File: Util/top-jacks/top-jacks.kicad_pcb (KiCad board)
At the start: 2 copper layers, 50.5 x 32.1 mm, 6 parts, among them J1 Screw_Terminal_01x02, J4 Barrel_Jack_Switch, J5 Screw_Terminal_01x06, J6 Screw_Terminal_01x02

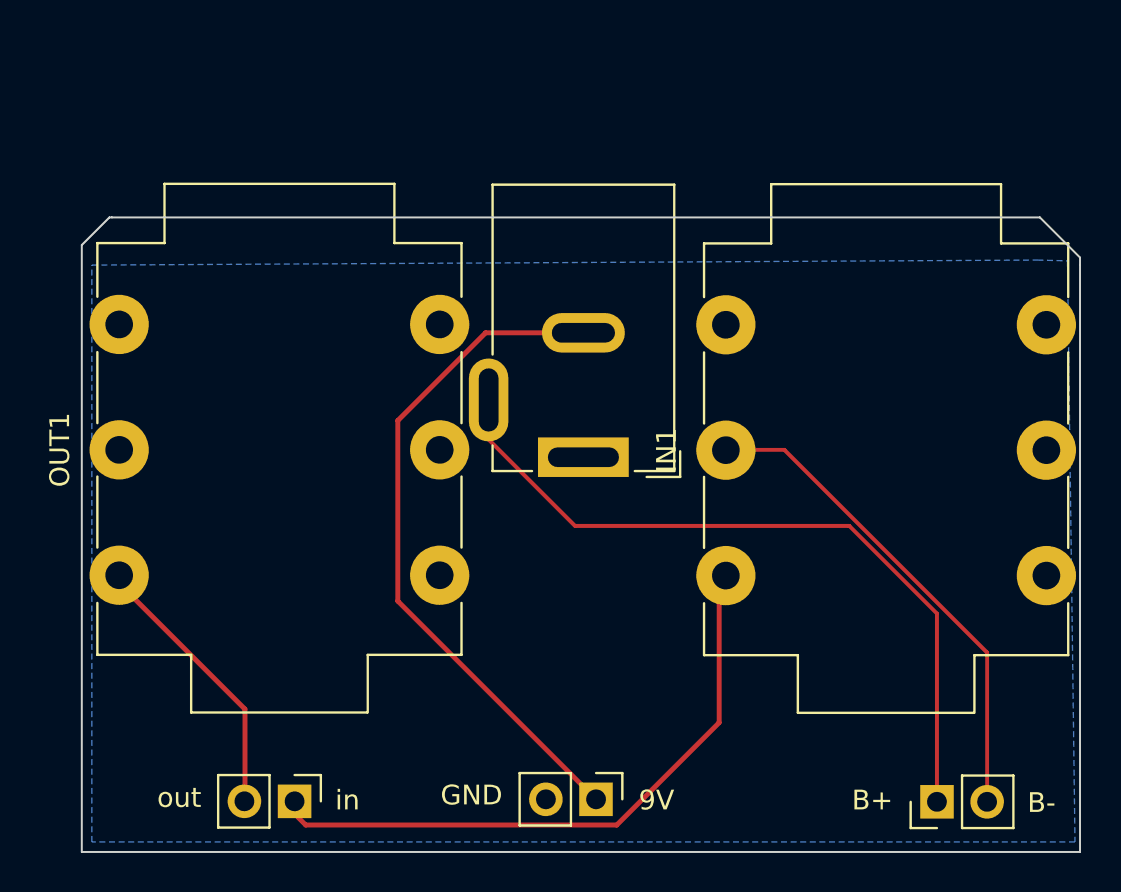
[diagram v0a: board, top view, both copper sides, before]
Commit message: replaced whiefuzz, and modified ejfuzzface
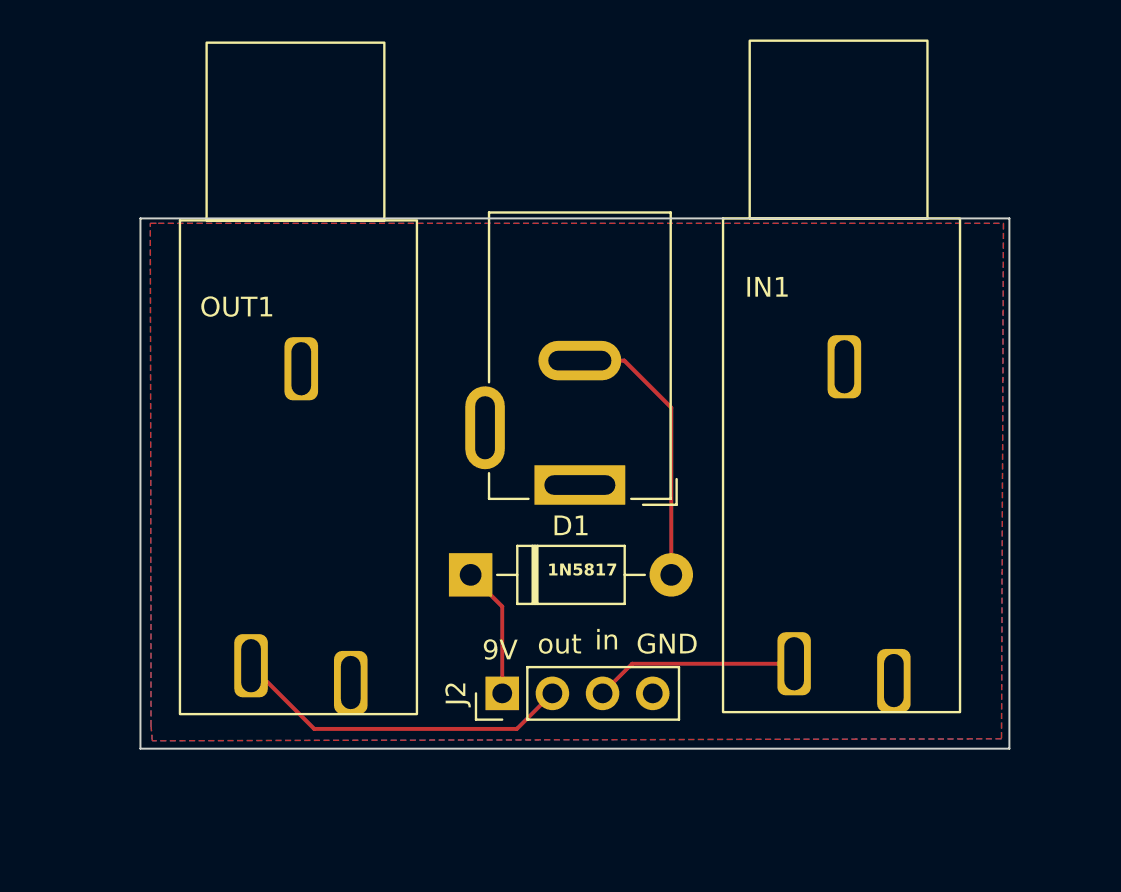
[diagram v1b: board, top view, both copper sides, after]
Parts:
- removed J1, J6: Screw_Terminal_01x02, Connector_PinHeader_2.54mm:PinHeader_1x02_P2.54mm_Vertical
- removed J5: Screw_Terminal_01x06, Connector_PinHeader_2.54mm:PinHeader_1x02_P2.54mm_Vertical
- added D1: 1N5817, Diode_THT:D_DO-41_SOD81_P10.16mm_Horizontal, F.Cu at (69.2, 94.3)
- added J2: Conn_01x04_Socket, Connector_PinHeader_2.54mm:PinHeader_1x04_P2.54mm_Vertical, F.Cu at (70.8, 100.3)
- IN1, OUT1: footprint Connector_Audio:Jack_6.35mm_Neutrik_NMJ6HCD2_Horizontal -> pedals:6.35mm-audio-jack
- moved OUT1 20.1 mm to (60.6, 76.4), turned to 0 degrees
- moved IN1 19.0 mm to (88.1, 76.3), turned to 0 degrees
- moved J4 1.42 mm to (74.8, 89.8)
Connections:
- J4 pad 2: 9v -> PWR
- J4 pad 3: B+ -> unconnected-(J4-Pad3)
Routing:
- net B+: track 41.6 -> 0.00 mm
- net 9v: track 34.6 -> 0.00 mm
- net B-: track 25.0 -> 0.00 mm
- net in: track 31.3 -> 10.3 mm
- net PWR: track 0.00 -> 14.1 mm
- net 9V: track 0.00 -> 6.66 mm
- net out: track 14.9 -> 17.3 mm
- added copper zone on F.Cu, net GND
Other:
- board size 50.5 x 32.1 mm -> 44 x 26.8 mm
- board text removed: "B+"
- board text removed: "B-"
